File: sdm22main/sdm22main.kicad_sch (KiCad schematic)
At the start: 8 parts, among them U1 Teensy4.1, U2 GPS_ADA746, U3 Accelerometer_ADXL335, U4 SN65HVD230_CAN_Transceiver

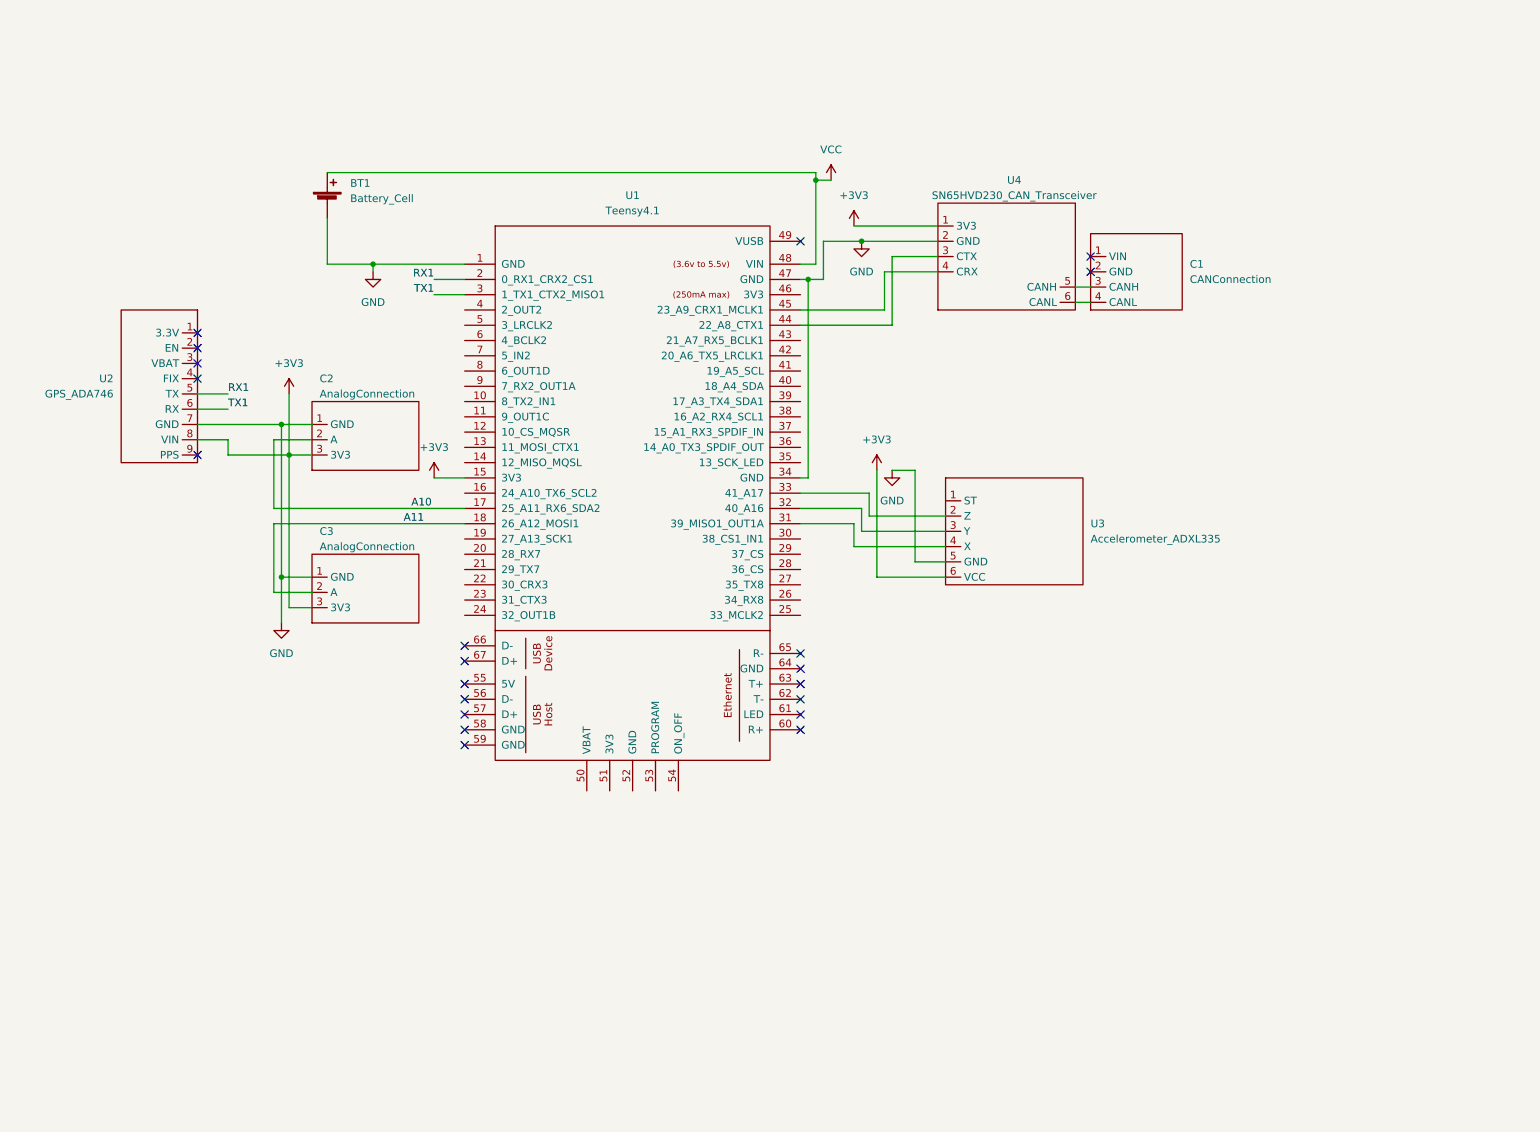
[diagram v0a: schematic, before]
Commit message: rewriting main schematic
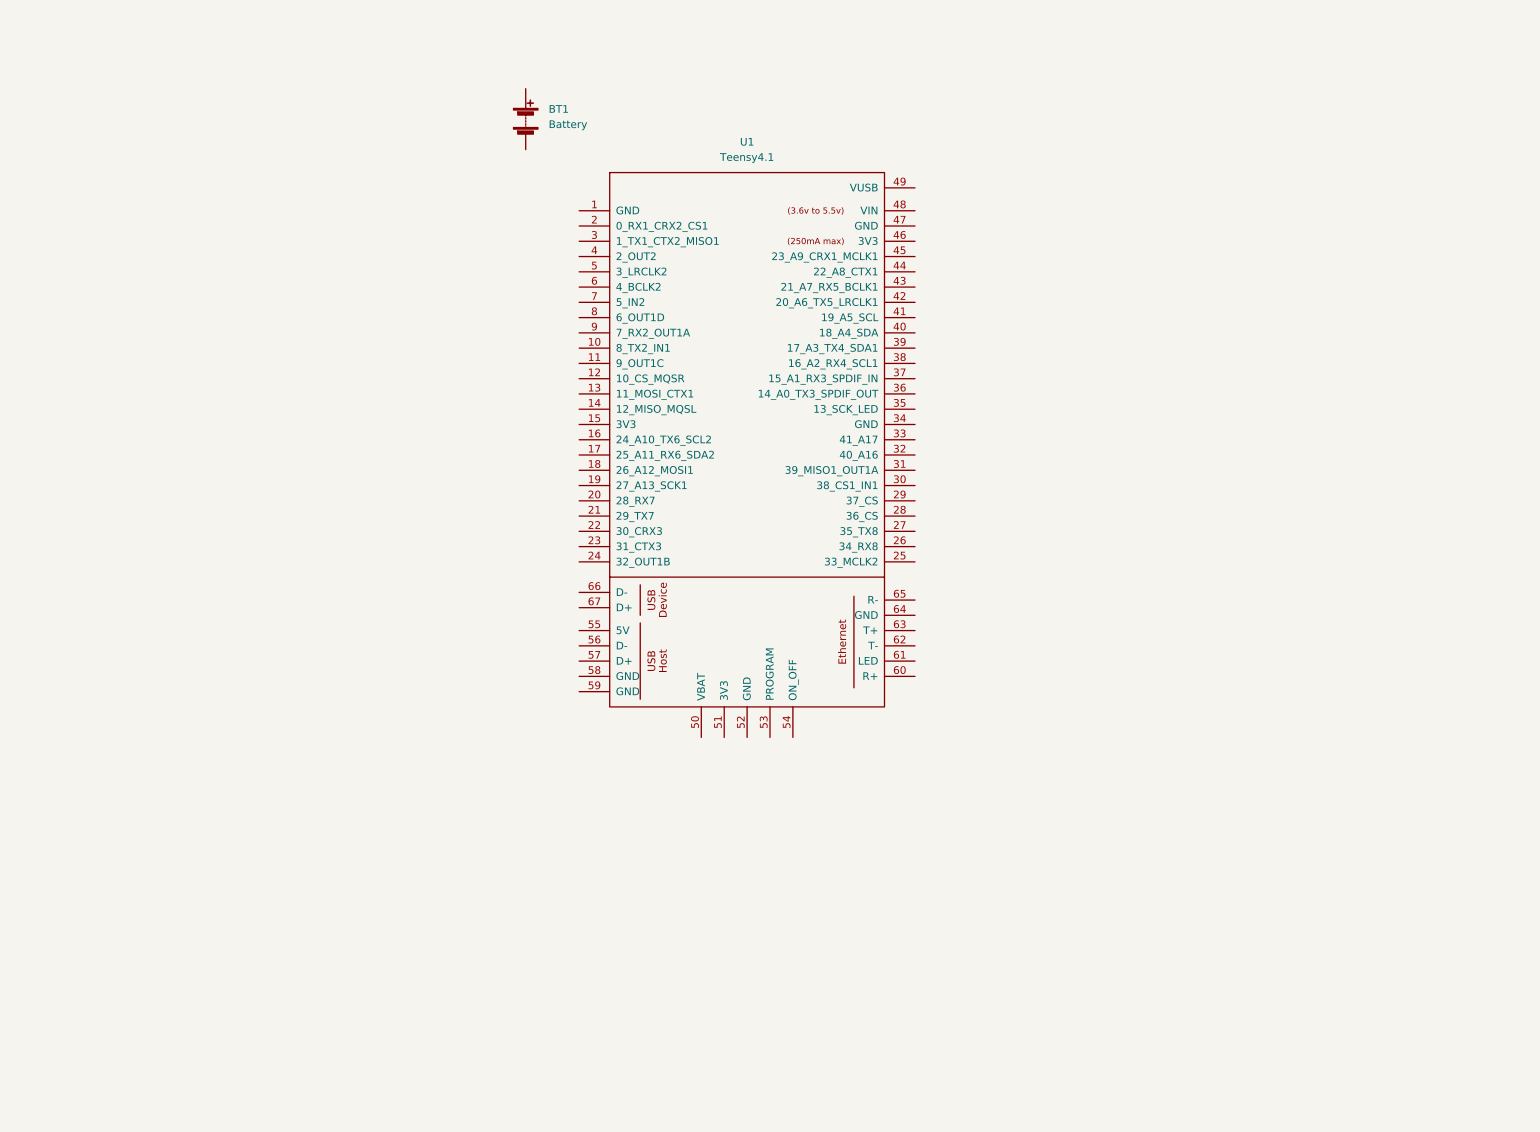
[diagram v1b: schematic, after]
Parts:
- removed BT1: Battery_Cell, Connector_PinHeader_1.00mm:PinHeader_1x02_P1.00mm_Horizontal, symbol Device:Battery_Cell
- removed C1: CANConnection, symbol SDM:CANConnection
- removed C2, C3: AnalogConnection, symbol SDM:AnalogConnection
- removed U2: GPS_ADA746, symbol SDM:GPS_ADA746
- removed U3: Accelerometer_ADXL335, symbol SDM:Accelerometer_ADXL335
- removed U4: SN65HVD230_CAN_Transceiver, symbol SDM:SN65HVD230_CAN_Transceiver
- added BT1: Battery, symbol Device:Battery
- U1: footprint Teensy:Teensy41 -> (none)
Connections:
- net +3V3: no longer names the net of U1.15 (3V3)
- net A10: no longer names the net of U1.17 (25_A11_RX6_SDA2)
- net A11: no longer names the net of U1.18 (26_A12_MOSI1)
- removed net GND: U1.1 (GND), U1.34 (GND), U1.47 (GND)
- net RX1: no longer names the net of U1.2 (0_RX1_CRX2_CS1)
- net TX1: no longer names the net of U1.3 (1_TX1_CTX2_MISO1)
- net VCC: no longer names the net of U1.48 (VIN)
- no-connect marks 21 -> 0
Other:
- company: Sun Devil Motorsports - DAQ -> Sun Devil Motorsports - Data Acquisition
- title: SDM-22 DAQ Main Module -> SDM-22 DAQ Main Board

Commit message: finished first draft of main board
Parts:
- added J1: CANConnection, symbol SDM:CANConnection
- added J2, J3, J4, J8: SerialConnection, SDM:4Wire_SerialConnector, symbol SDM:SerialConnection
- added J5, J6, J7: AnalogConnection, SDM:3Wire_AnalogConnector, symbol SDM:AnalogConnection
- added U2: GPS_ADA746, symbol SDM:GPS_ADA746
- added U3: SN65HVD230_CAN_Transceiver, symbol SDM:SN65HVD230_CAN_Transceiver
- added U4: Accelerometer_ADXL335, symbol SDM:Accelerometer_ADXL335
- BT1: footprint (none) -> Connector_PinSocket_2.54mm:PinSocket_1x02_P2.54mm_Vertical
- U1: footprint (none) -> Teensy:Teensy41
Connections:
- net VCC: now reaches BT1.1 (+)
- net VCC: now also U1.48 (VIN), J2.2 (VIN), J3.2 (VIN), J4.2 (VIN)
- net GND: now reaches BT1.2 (-)
- net GND: now also U1.1 (GND), U1.34 (GND), U1.47 (GND), J2.1 (GND), J3.1 (GND), J4.1 (GND), J5.1 (GND), J6.1 (GND), J7.1 (GND), J8.1 (GND), U2.7 (GND), U3.2 (GND), U4.5 (GND)
- net TX2: now reaches U1.10 (8_TX2_IN1)
- net TX2: now also J4.4 (RX)
- net A10: now reaches U1.16 (24_A10_TX6_SCL2)
- net A10: now also J6.2 (A)
- net A11: now reaches U1.17 (25_A11_RX6_SDA2)
- net A11: now also J5.2 (A)
- net RX1: now reaches U1.2 (0_RX1_CRX2_CS1)
- net RX1: now also U2.5 (TX)
- net RX7: now reaches U1.20 (28_RX7)
- net RX7: now also J3.3 (TX)
- net TX7: now reaches U1.21 (29_TX7)
- net TX7: now also J3.4 (RX)
- net RX8: now reaches U1.26 (34_RX8)
- net RX8: now also J2.3 (TX)
- net TX8: now reaches U1.27 (35_TX8)
- net TX8: now also J2.4 (RX)
- net TX1: now reaches U1.3 (1_TX1_CTX2_MISO1)
- net TX1: now also U2.6 (RX)
- net A14: now reaches U1.30 (38_CS1_IN1)
- net A14: now also J7.2 (A)
- net A15: now reaches U1.31 (39_MISO1_OUT1A)
- net A15: now also U4.4 (X)
- net A16: now reaches U1.32 (40_A16)
- net A16: now also U4.3 (Y)
- net A17: now reaches U1.33 (41_A17)
- net A17: now also U4.2 (Z)
- net TX3: now reaches U1.36 (14_A0_TX3_SPDIF_OUT)
- net TX3: now also J8.4 (RX)
- net RX3: now reaches U1.37 (15_A1_RX3_SPDIF_IN)
- net RX3: now also J8.3 (TX)
- net CTX1: now reaches U1.44 (22_A8_CTX1)
- net CTX1: now also U3.3 (CTX)
- net CRX1: now reaches U1.45 (23_A9_CRX1_MCLK1)
- net CRX1: now also U3.4 (CRX)
- net +3V3: now reaches U1.46 (3V3)
- net +3V3: now also J5.3 (3V3), J6.3 (3V3), J7.3 (3V3), J8.2 (VIN), U2.8 (VIN), U3.1 (3V3), U4.6 (VCC)
- net RX2: now reaches U1.9 (7_RX2_OUT1A)
- net RX2: now also J4.3 (TX)
- new net: J1.3 (CANH), U3.5 (CANH)
- new net: J1.4 (CANL), U3.6 (CANL)
- no-connect marks 0 -> 22
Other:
- moved on the sheet: BT1, U1

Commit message: first draft main board
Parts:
- J1: footprint (none) -> SDM:4Wire_CANConnector
- U2: footprint (none) -> SDM:ADA746_Socket_P2.54mm_Vertical
- U3: footprint (none) -> SDM:SN65HVD230_Socket_P2.54mm_Vertical
- U4: footprint (none) -> SDM:ADXL335_Socket_P2.54mm_Vertical
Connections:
- net A14: now also U4.4 (X); no longer J7.2 (A)
- net A15: now also U4.3 (Y); no longer U4.4 (X)
- net A16: now also U4.2 (Z); no longer U4.3 (Y)
- net A17: now also J7.2 (A); no longer U4.2 (Z)
- net RX1: now also J4.3 (TX); no longer U2.5 (TX)
- net RX2: now also J3.3 (TX); no longer J4.3 (TX)
- net RX7: now also U2.5 (TX); no longer J3.3 (TX)
- net TX1: now also J4.4 (RX); no longer U2.6 (RX)
- net TX2: now also J3.4 (RX); no longer J4.4 (RX)
- net TX7: now also U2.6 (RX); no longer J3.4 (RX)
- net TX5: now reaches U1.42 (20_A6_TX5_LRCLK1)
- net TX5: now also J2.4 (RX)
- net RX5: now reaches U1.43 (21_A7_RX5_BCLK1)
- net RX5: now also J2.3 (TX)
- net RX8: no longer names the net of U1.26 (34_RX8)
- net RX8: no longer J2.3 (TX)
- net TX8: no longer names the net of U1.27 (35_TX8)
- net TX8: no longer J2.4 (RX)
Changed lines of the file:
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@@
+    (stroke (width 0) (type default) (color 0 0 0 0))
+  )
+  (wire (pts (xy 175.26 57.15) (xy 176.53 57.15))
     (stroke (width 0) (type default) (color 0 0 0 0))
   )
@@
     (stroke (width 0) (type default) (color 0 0 0 0))
   )
-  (wire (pts (xy 176.53 54.61) (xy 175.26 54.61))
-    (stroke (width 0) (type default) (color 0 0 0 0))
-  )
   (wire (pts (xy 189.23 59.69) (xy 189.23 77.47))
     (stroke (width 0) (type default) (color 0 0 0 0))
@@
     (stroke (width 0) (type default) (color 0 0 0 0))
   )
+  (wire (pts (xy 175.26 59.69) (xy 176.53 59.69))
+    (stroke (width 0) (type default) (color 0 0 0 0))
+  )
   (wire (pts (xy 152.4 54.61) (xy 143.51 54.61))
     (stroke (width 0) (type default) (color 0 0 0 0))
@@
     (stroke (width 0) (type default) (color 0 0 0 0))
   )
-  (wire (pts (xy 214.63 57.15) (xy 218.44 57.15))
-    (stroke (width 0) (type default) (color 0 0 0 0))
-  )
   (wire (pts (xy 19.05 38.1) (xy 19.05 36.83))
     (stroke (width 0) (type default) (color 0 0 0 0))
@@
     (stroke (width 0) (type default) (color 0 0 0 0))
   )
-  (wire (pts (xy 176.53 57.15) (xy 175.26 57.15))
-    (stroke (width 0) (type default) (color 0 0 0 0))
-  )
   (wire (pts (xy 214.63 41.91) (xy 217.17 41.91))
     (stroke (width 0) (type default) (color 0 0 0 0))
@@
     (stroke (width 0) (type default) (color 0 0 0 0))
   )
+  (wire (pts (xy 214.63 57.15) (xy 217.17 57.15))
+    (stroke (width 0) (type default) (color 0 0 0 0))
+  )
   (wire (pts (xy 147.32 59.69) (xy 152.4 59.69))
     (stroke (width 0) (type default) (color 0 0 0 0))
@@
     (stroke (width 0) (type default) (color 0 0 0 0))
   )
+  (wire (pts (xy 175.26 54.61) (xy 176.53 54.61))
+    (stroke (width 0) (type default) (color 0 0 0 0))
+  )
   (wire (pts (xy 133.35 147.32) (xy 138.43 147.32))
     (stroke (width 0) (type default) (color 0 0 0 0))
@@
     (stroke (width 0) (type default) (color 0 0 0 0))
   )
-  (wire (pts (xy 176.53 59.69) (xy 175.26 59.69))
-    (stroke (width 0) (type default) (color 0 0 0 0))
-  )
   (wire (pts (xy 161.29 111.76) (xy 166.37 111.76))
     (stroke (width 0) (type default) (color 0 0 0 0))
@@
     (stroke (width 0) (type default) (color 0 0 0 0))
   )
-  (label "A16" (at 176.53 57.15 0)
+  (label "A16" (at 176.53 54.61 0)
     (effects (font (size 1.27 1.27)) (justify left bottom))
   )
@@
     (effects (font (size 1.27 1.27)) (justify left bottom))
   )
-  (label "RX2" (at 133.35 161.29 0)
+  (label "TX5" (at 133.35 129.54 0)
+    (effects (font (size 1.27 1.27)) (justify left bottom))
+  )
+  (label "RX1" (at 133.35 161.29 0)
     (effects (font (size 1.27 1.27)) (justify left bottom))
   )
@@
     (effects (font (size 1.27 1.27)) (justify left bottom))
   )
-  (label "RX8" (at 96.52 107.95 0)
-    (effects (font (size 1.27 1.27)) (justify left bottom))
-  )
   (label "A14" (at 96.52 97.79 0)
     (effects (font (size 1.27 1.27)) (justify left bottom))
@@
     (effects (font (size 1.27 1.27)) (justify left bottom))
   )
-  (label "RX8" (at 133.35 127 0)
+  (label "RX5" (at 133.35 127 0)
+    (effects (font (size 1.27 1.27)) (justify left bottom))
+  )
+  (label "RX2" (at 133.35 144.78 0)
     (effects (font (size 1.27 1.27)) (justify left bottom))
   )
@@
     (effects (font (size 1.27 1.27)) (justify left bottom))
   )
-  (label "A17" (at 176.53 54.61 0)
+  (label "RX5" (at 96.52 64.77 0)
+    (effects (font (size 1.27 1.27)) (justify left bottom))
+  )
+  (label "A17" (at 217.17 57.15 0)
     (effects (font (size 1.27 1.27)) (justify left bottom))
   )
@@
     (effects (font (size 1.27 1.27)) (justify left bottom))
   )
+  (label "RX7" (at 168.91 34.29 0)
+    (effects (font (size 1.27 1.27)) (justify left bottom))
+  )
+  (label "TX2" (at 133.35 147.32 0)
+    (effects (font (size 1.27 1.27)) (justify left bottom))
+  )
   (label "A11" (at 217.17 25.4 0)
     (effects (font (size 1.27 1.27)) (justify left bottom))
   )
-  (label "TX8" (at 133.35 129.54 0)
-    (effects (font (size 1.27 1.27)) (justify left bottom))
-  )
   (label "TX3" (at 96.52 82.55 0)
     (effects (font (size 1.27 1.27)) (justify left bottom))
   )
-  (label "TX8" (at 96.52 105.41 0)
-    (effects (font (size 1.27 1.27)) (justify left bottom))
-  )
-  (label "A15" (at 176.53 59.69 0)
+  (label "A15" (at 176.53 57.15 0)
     (effects (font (size 1.27 1.27)) (justify left bottom))
   )
@@
     (effects (font (size 1.27 1.27)) (justify left bottom))
   )
-  (label "TX7" (at 133.35 147.32 0)
-    (effects (font (size 1.27 1.27)) (justify left bottom))
-  )
-  (label "A14" (at 218.44 57.15 0)
+  (label "A14" (at 176.53 59.69 0)
     (effects (font (size 1.27 1.27)) (justify left bottom))
   )
@@
     (effects (font (size 1.27 1.27)) (justify left bottom))
   )
-  (label "RX7" (at 133.35 144.78 0)
-    (effects (font (size 1.27 1.27)) (justify left bottom))
-  )
-  (label "TX1" (at 147.32 36.83 0)
-    (effects (font (size 1.27 1.27)) (justify left bottom))
-  )
-  (label "RX1" (at 168.91 34.29 0)
+  (label "TX5" (at 96.52 67.31 0)
     (effects (font (size 1.27 1.27)) (justify left bottom))
   )
@@
     (effects (font (size 1.27 1.27)) (justify left bottom))
   )
-  (label "TX2" (at 133.35 163.83 0)
+  (label "TX1" (at 133.35 163.83 0)
     (effects (font (size 1.27 1.27)) (justify left bottom))
   )
@@
     (effects (font (size 1.27 1.27)) (justify left bottom))
   )
+  (label "TX7" (at 147.32 36.83 0)
+    (effects (font (size 1.27 1.27)) (justify left bottom))
+  )
   (label "RX3" (at 96.52 80.01 0)
     (effects (font (size 1.27 1.27)) (justify left bottom))
+  )
+  (symbol (lib_id "SDM:CANConnection") (at 172.72 99.06 0) (unit 1)
+    (in_bom yes) (on_board yes) (fields_autoplaced)
+    (property "Reference" "J1" (id 0) (at 182.88 105.4099 0)
+      (effects (font (size 1.27 1.27)) (justify left))
+    )
+    (property "Value" "CANConnection" (id 1) (at 182.88 107.9499 0)
+      (effects (font (size 1.27 1.27)) (justify left))
+    )
+    (property "Footprint" "SDM:4Wire_CANConnector" (id 2) (at 172.72 99.06 0)
+      (effects (font (size 1.27 1.27)) hide)
+    )
+    (property "Datasheet" "" (id 3) (at 172.72 99.06 0)
+      (effects (font (size 1.27 1.27)) hide)
+    )
+    (pin "1")
+    (pin "2")
+    (pin "3")
+    (pin "4")
   )
   (symbol (lib_id "power:+3V3") (at 132.08 99.06 0) (unit 1)
@@
     (property "Reference" "U4" (id 0) (at 163.83 45.72 0))
     (property "Value" "Accelerometer_ADXL335" (id 1) (at 163.83 48.26 0))
-    (property "Footprint" "" (id 2) (at 158.75 50.8 0)
+    (property "Footprint" "SDM:ADXL335_Socket_P2.54mm_Vertical" (id 2) (at 158.75 50.8 0)
       (effects (font (size 1.27 1.27)) hide)
     )
@@
     (property "Reference" "U2" (id 0) (at 159.385 20.32 0))
     (property "Value" "GPS_ADA746" (id 1) (at 159.385 22.86 0))
-    (property "Footprint" "" (id 2) (at 158.75 24.13 0)
+    (property "Footprint" "SDM:ADA746_Socket_P2.54mm_Vertical" (id 2) (at 158.75 24.13 0)
       (effects (font (size 1.27 1.27)) hide)
     )
@@
     )
     (property "Datasheet" "" (id 3) (at 204.47 64.77 0)
-      (effects (font (size 1.27 1.27)) hide)
-    )
-    (pin "1")
-    (pin "2")
-    (pin "3")
-    (pin "4")
-  )
-  (symbol (lib_id "SDM:CANConnection") (at 172.72 99.06 0) (unit 1)
-    (in_bom yes) (on_board yes) (fields_autoplaced)
-    (property "Reference" "J1" (id 0) (at 182.88 105.4099 0)
-      (effects (font (size 1.27 1.27)) (justify left))
-    )
-    (property "Value" "CANConnection" (id 1) (at 182.88 107.9499 0)
-      (effects (font (size 1.27 1.27)) (justify left))
-    )
-    (property "Footprint" "" (id 2) (at 172.72 99.06 0)
-      (effects (font (size 1.27 1.27)) hide)
-    )
-    (property "Datasheet" "" (id 3) (at 172.72 99.06 0)
       (effects (font (size 1.27 1.27)) hide)
     )
@@
     (property "Reference" "U3" (id 0) (at 149.86 90.17 0))
     (property "Value" "SN65HVD230_CAN_Transceiver" (id 1) (at 149.86 92.71 0))
-    (property "Footprint" "" (id 2) (at 147.32 93.98 0)
+    (property "Footprint" "SDM:SN65HVD230_Socket_P2.54mm_Vertical" (id 2) (at 147.32 93.98 0)
       (effects (font (size 1.27 1.27)) hide)
     )
@@
       (reference "BT1") (unit 1) (value "Battery") (footprint "Connector_PinSocket_2.54mm:PinSocket_1x02_P2.54mm_Vertical")
     )
-    (path "/b6455abf-6892-4ba2-96f8-74bd15e80e11"
-      (reference "J1") (unit 1) (value "CANConnection") (footprint "")
+    (path "/01c740b8-c613-452b-aaa0-8aafa1cc516e"
+      (reference "J1") (unit 1) (value "CANConnection") (footprint "SDM:4Wire_CANConnector")
     )
     (path "/73394da4-d0fb-4a0a-9f03-1154c6cfec44"
@@
     )
     (path "/54ab07d5-431a-4bf2-b5f7-04869fadbebd"
-      (reference "U2") (unit 1) (value "GPS_ADA746") (footprint "")
+      (reference "U2") (unit 1) (value "GPS_ADA746") (footprint "SDM:ADA746_Socket_P2.54mm_Vertical")
     )
     (path "/f40ba485-8c78-4c62-b563-bf913d16f507"
-      (reference "U3") (unit 1) (value "SN65HVD230_CAN_Transceiver") (footprint "")
+      (reference "U3") (unit 1) (value "SN65HVD230_CAN_Transceiver") (footprint "SDM:SN65HVD230_Socket_P2.54mm_Vertical")
     )
     (path "/47ca04bb-6b04-4be8-8871-71c72a75cbae"
-      (reference "U4") (unit 1) (value "Accelerometer_ADXL335") (footprint "")
-    )
-  )
+      (reference "U4") (unit 1) (value "Accelerometer_ADXL335") (footprint "SDM:ADXL335_Socket_P2.54mm_Vertical")
+    )
+  )

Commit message: rev 1.1 for main board, a lot simpler
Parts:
- J1: footprint SDM:4Wire_CANConnector -> SDM:2Wire_CANConnector
- renumbered J5 to J2, J6 to J3, J3 to J4, J4 to J5, J2 to J6, J8 to J7, J7 to J8, U3 to U2, U2 to U3
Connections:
- net +3V3: no longer J2.3 (3V3), J3.3 (3V3), U2.1 (3V3)
- net at J1.1 (CANH): now also U2.5 (CANH)
- net at J1.2 (CANL): now also U2.6 (CANL)
- net +3.3VP: now reaches U1.15 (3V3)
- net +3.3VP: now also J2.3 (3V3), J3.3 (3V3), U2.1 (3V3)
- net CRX3: now reaches U1.22 (30_CRX3)
- net CRX3: now also U2.4 (CRX)
- net CTX3: now reaches U1.23 (31_CTX3)
- net CTX3: now also U2.3 (CTX)
- net RX8: now reaches U1.26 (34_RX8)
- net RX8: now also U3.5 (TX)
- net TX8: now reaches U1.27 (35_TX8)
- net TX8: now also U3.6 (RX)
- net CRX1: no longer names the net of U1.45 (23_A9_CRX1_MCLK1)
- net CRX1: no longer U2.4 (CRX)
- net CTX1: no longer names the net of U1.44 (22_A8_CTX1)
- net CTX1: no longer U2.3 (CTX)
- net RX7: no longer names the net of U1.20 (28_RX7)
- net RX7: no longer U3.5 (TX)
- net TX7: no longer names the net of U1.21 (29_TX7)
- net TX7: no longer U3.6 (RX)
- no-connect marks 22 -> 20
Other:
- moved on the sheet: J2, J3, J4, J5, J6, J7, J8, U2, U3, U4
